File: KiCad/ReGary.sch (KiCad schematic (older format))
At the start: 10 parts, among them U4 SN74CBT16210, U5 SN74CBT16210, U6 SN74CBT16210, U7 SN74CBT16210, U8 PLCC_84_plug, U9 PLCC_84_plug

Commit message: Placement of caps and more routing
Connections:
- net GND: now also U6.13 (2A1)
- no-connect marks 1 -> 2
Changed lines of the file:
@@
 Text GLabel 8150 4800 2    50   Output ~ 0
 PWRUP_FPGA
+Text GLabel 7150 5000 0    50   Input ~ 0
+GND
+NoConn ~ 8150 5100
 $EndSCHEMATC

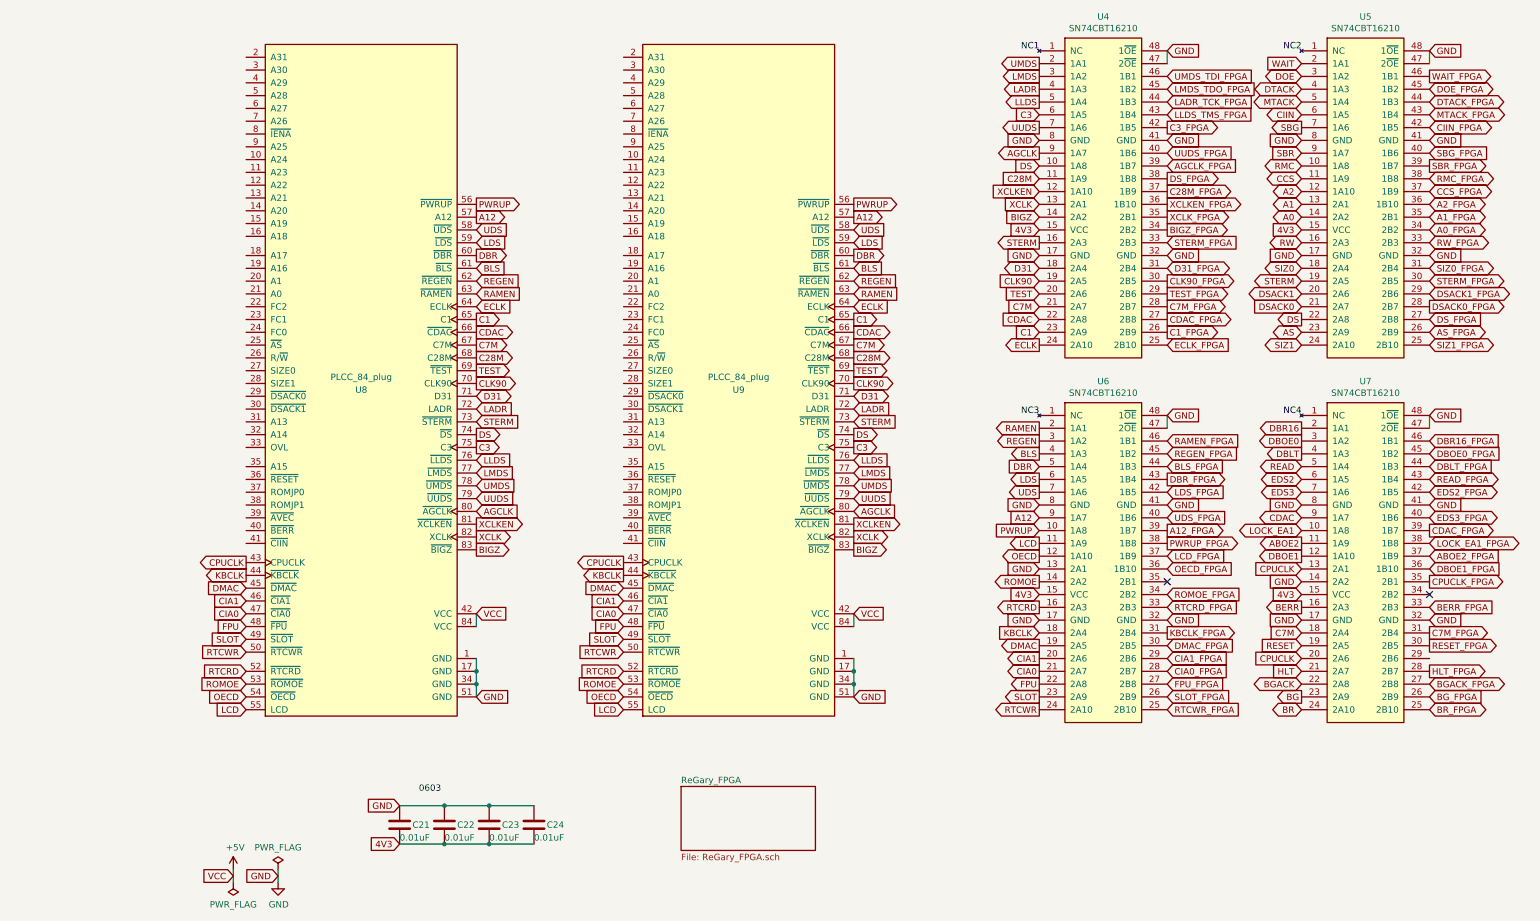
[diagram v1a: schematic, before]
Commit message: More pin assignments and routing
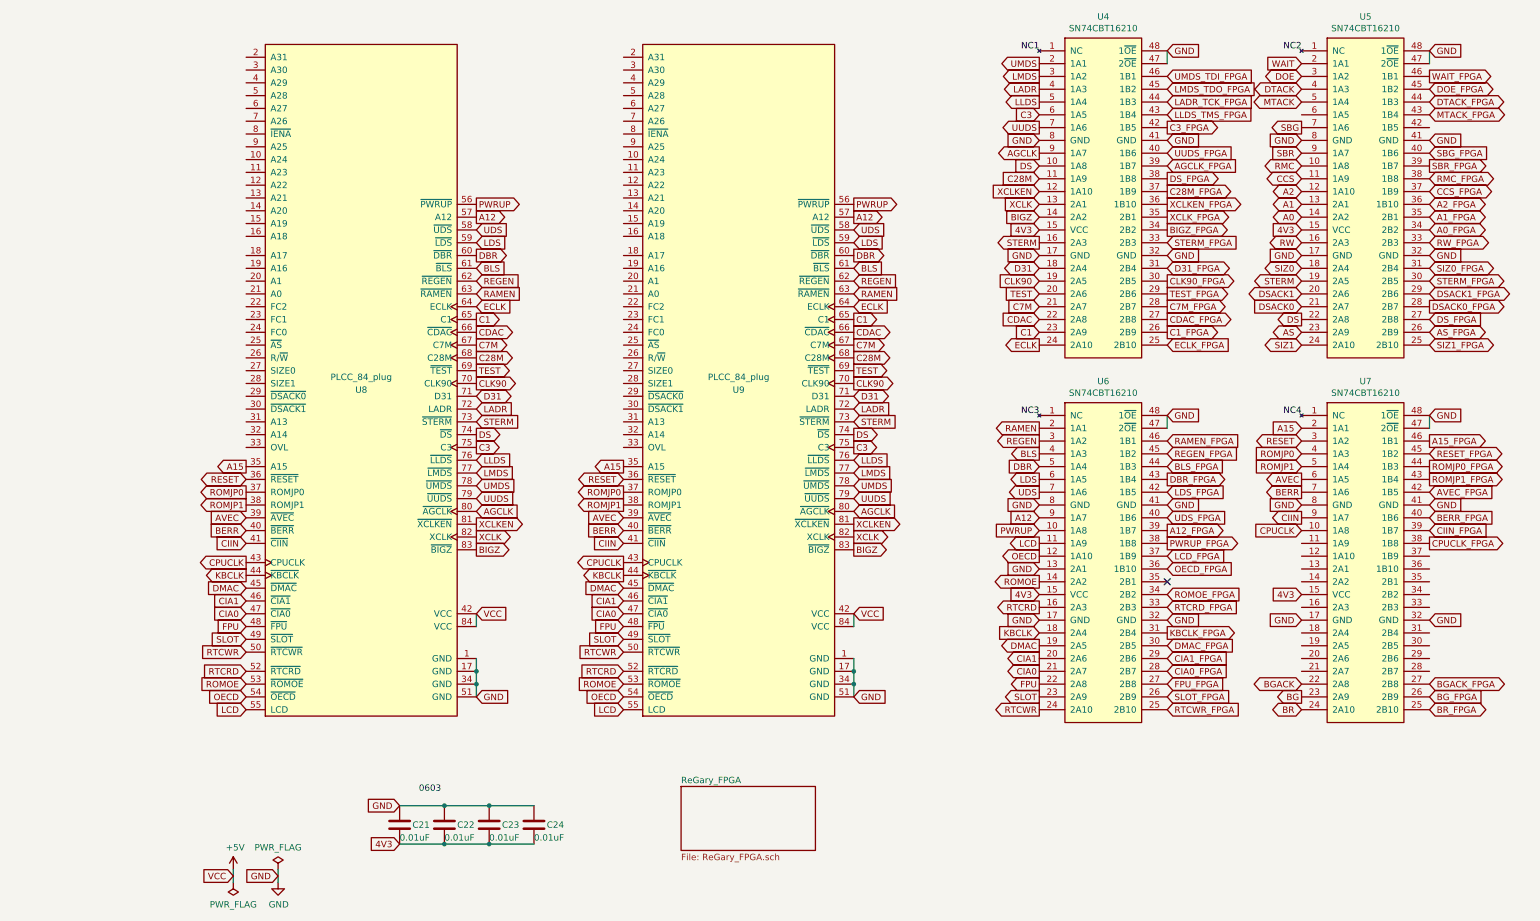
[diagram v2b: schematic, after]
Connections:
- net DBLT is gone; now on net ROMJP0: U7.4 (1A3)
- net DBOE0 is gone; now on net RESET: U7.3 (1A2)
- net DBOE0_FPGA is gone; now on net RESET_FPGA: U7.45 (1B2)
- net DBR16 is gone; now on net A15: U7.2 (1A1)
- net EDS2 is gone; now on net AVEC: U7.6 (1A5)
- net EDS3 is gone; now on net BERR: U7.7 (1A6)
- net EDS3_FPGA is gone; now on net BERR_FPGA: U7.40 (1B6)
- net LOCK_EA1 is gone; now on net CPUCLK: U7.10 (1A8)
- net LOCK_EA1_FPGA is gone; now on net CPUCLK_FPGA: U7.38 (1B8)
- net READ is gone; now on net ROMJP1: U7.5 (1A4)
- net BERR: now also U8.40 (~BERR), U9.40 (~BERR); no longer U7.16 (2A3)
- net BERR_FPGA: no longer U7.33 (2B3)
- net C7M: no longer U7.18 (2A4)
- net C7M_FPGA: no longer U7.31 (2B4)
- net CDAC: no longer U7.9 (1A7)
- net CDAC_FPGA: no longer U7.39 (1B7)
- net CIIN: now also U7.9 (1A7), U8.41 (~CIIN), U9.41 (~CIIN); no longer U5.6 (1A5)
- net CIIN_FPGA: now also U7.39 (1B7); no longer U5.42 (1B5)
- net CPUCLK: no longer U7.13 (2A1), U7.20 (2A6)
- net CPUCLK_FPGA: no longer U7.35 (2B1)
- net GND: no longer U7.14 (2A2)
- net RESET: now also U8.36 (~RESET), U9.36 (~RESET); no longer U7.19 (2A5)
- net RESET_FPGA: no longer U7.30 (2B5)
- net A15: now reaches U9.35 (A15)
- net A15: now also U8.35 (A15)
- net ROMJP0: now reaches U9.37 (ROMJP0)
- net ROMJP0: now also U8.37 (ROMJP0)
- net ROMJP1: now reaches U9.38 (ROMJP1)
- net ROMJP1: now also U8.38 (ROMJP1)
- net AVEC: now reaches U9.39 (~AVEC)
- net AVEC: now also U8.39 (~AVEC)
- net ABOE2: no longer names the net of U7.11 (1A9)
- net ABOE2_FPGA: no longer names the net of U7.37 (1B9)
- net DBLT_FPGA renamed ROMJP0_FPGA
- net DBOE1: no longer names the net of U7.12 (1A10)
- net DBOE1_FPGA: no longer names the net of U7.36 (1B10)
- net DBR16_FPGA renamed A15_FPGA
- net EDS2_FPGA renamed AVEC_FPGA
- net HLT: no longer names the net of U7.21 (2A7)
- net HLT_FPGA: no longer names the net of U7.28 (2B7)
- net READ_FPGA renamed ROMJP1_FPGA
- no-connect marks 2 -> 1
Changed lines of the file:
@@
 Text GLabel 10200 1450 2    50   BiDi ~ 0
 MTACK_FPGA
-Text GLabel 10200 1550 2    50   BiDi ~ 0
-CIIN_FPGA
 Text GLabel 10200 1850 2    50   Output ~ 0
 SBR_FPGA
@@
 Text GLabel 8150 4300 2    50   Output ~ 0
 DBR_FPGA
-Text GLabel 10200 4000 2    50   Input ~ 0
-DBR16_FPGA
-Text GLabel 10200 4100 2    50   Input ~ 0
-DBOE0_FPGA
-Text GLabel 10200 4300 2    50   BiDi ~ 0
-READ_FPGA
-Text GLabel 10200 4400 2    50   BiDi ~ 0
-EDS2_FPGA
-Text GLabel 10200 4600 2    50   BiDi ~ 0
-EDS3_FPGA
-Text GLabel 10200 4700 2    50   Output ~ 0
-CDAC_FPGA
-Text GLabel 10200 4800 2    50   BiDi ~ 0
-LOCK_EA1_FPGA
-Text GLabel 10200 4900 2    50   Input ~ 0
-ABOE2_FPGA
-Text GLabel 10200 5000 2    50   Input ~ 0
-DBOE1_FPGA
-Text GLabel 10200 5300 2    50   Input ~ 0
-BERR_FPGA
-Text GLabel 10200 4200 2    50   Input ~ 0
-DBLT_FPGA
-Text GLabel 10200 5600 2    50   Output ~ 0
-RESET_FPGA
-Text GLabel 10200 5500 2    50   Output ~ 0
-C7M_FPGA
-Text GLabel 10200 5800 2    50   Output ~ 0
-HLT_FPGA
-Text GLabel 10200 5100 2    50   Output ~ 0
+Text GLabel 10200 4800 2    50   Output ~ 0
 CPUCLK_FPGA
 Text GLabel 10200 5900 2    50   BiDi ~ 0
@@
 Text GLabel 9200 1550 0    50   Output ~ 0
 SBG
-Text GLabel 9200 1450 0    50   BiDi ~ 0
-CIIN
 Text GLabel 9200 1350 0    50   BiDi ~ 0
 MTACK
@@
 Text GLabel 9200 5900 0    50   BiDi ~ 0
 BGACK
-Text GLabel 9200 5800 0    50   Input ~ 0
-HLT
-Text GLabel 9200 5300 0    50   Output ~ 0
-BERR
-Text GLabel 9200 5600 0    50   Input ~ 0
-RESET
-Text GLabel 9200 5700 0    50   Input ~ 0
-CPUCLK
-Text GLabel 9200 5500 0    50   Input ~ 0
-C7M
-Text GLabel 9200 4600 0    50   BiDi ~ 0
-CDAC
-Text GLabel 9200 4900 0    50   Output ~ 0
-DBOE1
-Text GLabel 9200 4000 0    50   Output ~ 0
-DBOE0
-Text GLabel 9200 3900 0    50   Output ~ 0
-DBR16
-Text GLabel 9200 4100 0    50   Output ~ 0
-DBLT
-Text GLabel 9200 4200 0    50   BiDi ~ 0
-READ
-Text GLabel 9200 4300 0    50   BiDi ~ 0
-EDS2
-Text GLabel 9200 4400 0    50   BiDi ~ 0
-EDS3
-Text GLabel 9200 4700 0    50   BiDi ~ 0
-LOCK_EA1
-Text GLabel 9200 4800 0    50   Output ~ 0
-ABOE2
 Text GLabel 2750 2450 2    50   Input ~ 0
 LDS
@@
 Text GLabel 5700 5350 2    50   Input ~ 0
 VCC
-Text GLabel 9200 5100 0    50   Input ~ 0
-GND
 Text GLabel 8150 1550 2    50   Output ~ 0
 C3_FPGA
@@
 Text GLabel 10200 2950 2    50   Output ~ 0
 DSACK0_FPGA
-NoConn ~ 10200 5200
 $Sheet
 S 4350 6700 1050 500
@@
 Text GLabel 5700 2450 2    50   Input ~ 0
 LDS
-Text GLabel 9200 5000 0    50   Input ~ 0
+Text GLabel 9200 4700 0    50   Input ~ 0
 CPUCLK
 Text GLabel 7150 5500 0    50   Input ~ 0
@@
 GND
 NoConn ~ 8150 5100
+Text GLabel 950  4800 0    50   Input ~ 0
+CIIN
+Text GLabel 9200 4600 0    50   Output ~ 0
+CIIN
+Text GLabel 3900 4800 0    50   Input ~ 0
+CIIN
+Text GLabel 10200 4700 2    50   Input ~ 0
+CIIN_FPGA
+Text GLabel 950  4700 0    50   Input ~ 0
+BERR
+Text GLabel 9200 4400 0    50   Output ~ 0
+BERR
+Text GLabel 10200 4600 2    50   Input ~ 0
+BERR_FPGA
+Text GLabel 3900 4700 0    50   Input ~ 0
+BERR
+Text GLabel 950  4600 0    50   Input ~ 0
+AVEC
+Text GLabel 950  4500 0    50   Output ~ 0
+ROMJP1
+Text GLabel 950  4400 0    50   Output ~ 0
+ROMJP0
+Text GLabel 950  4300 0    50   BiDi ~ 0
+RESET
+Text GLabel 950  4200 0    50   Output ~ 0
+A15
+Text GLabel 3900 4600 0    50   Input ~ 0
+AVEC
+Text GLabel 9200 4300 0    50   Output ~ 0
+AVEC
+Text GLabel 3900 4500 0    50   Output ~ 0
+ROMJP1
+Text GLabel 3900 4400 0    50   Output ~ 0
+ROMJP0
+Text GLabel 3900 4300 0    50   BiDi ~ 0
+RESET
+Text GLabel 3900 4200 0    50   Output ~ 0
+A15
+Text GLabel 9200 4200 0    50   Input ~ 0
+ROMJP1
+Text GLabel 9200 4100 0    50   Input ~ 0
+ROMJP0
+Text GLabel 9200 4000 0    50   BiDi ~ 0
+RESET
+Text GLabel 9200 3900 0    50   Input ~ 0
+A15
+Text GLabel 10200 4400 2    50   Input ~ 0
+AVEC_FPGA
+Text GLabel 10200 4300 2    50   Output ~ 0
+ROMJP1_FPGA
+Text GLabel 10200 4200 2    50   Output ~ 0
+ROMJP0_FPGA
+Text GLabel 10200 4100 2    50   BiDi ~ 0
+RESET_FPGA
+Text GLabel 10200 4000 2    50   Output ~ 0
+A15_FPGA
 $EndSCHEMATC
